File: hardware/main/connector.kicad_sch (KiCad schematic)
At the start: 22 parts, among them J11 TF-01A, J3 Conn_01x04, J4 Conn_01x04, J5 Conn_01x04, J6 Conn_01x04, J7 Conn_01x10, J7b Conn_01x08, J8 Conn_01x06, J9 Conn_01x04

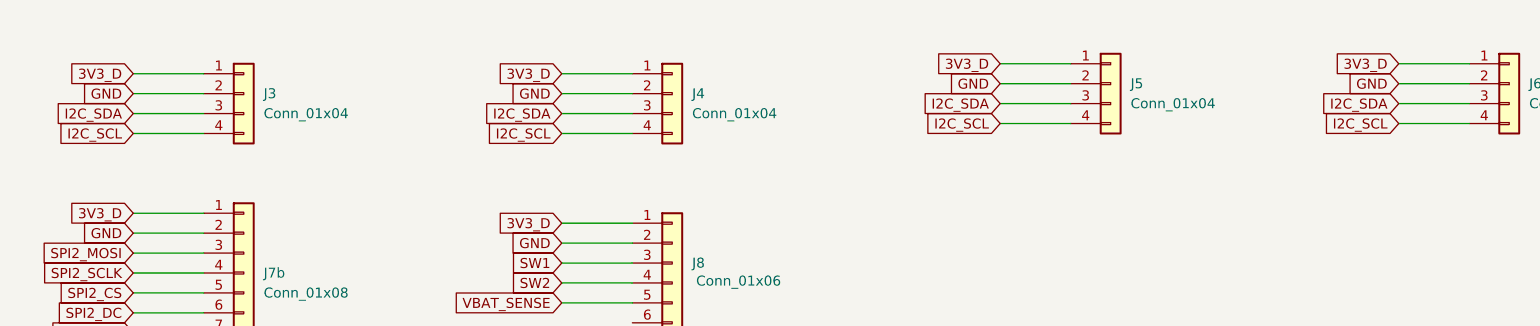
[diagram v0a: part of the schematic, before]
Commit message: hardware+tools: brochage Qwiic J3-J6 applique, outils de verification
- connector.kicad_sch : patch Qwiic reporte dans le projet (pin 1 = GND,
  2 = 3V3_D, 3 = SDA, 4 = SCL). Verifie par netlist sur les 4 connecteurs.
  Solde le point bloquant H2 de l'audit 2026-09-23.
- tools/kicad_netlist.py : reconstruit la netlist depuis les .kicad_sch
  (wires, junctions, global labels, pins transformees). Le script de l'audit
  n'avait pas ete commite et avait ete perdu ; il l'est desormais.
  91,9 % des 430 pins raccordees, 123 nets. Options --ref / --net / --all.
- tools/pdf_text.py : extraction de texte PDF en stdlib seule (ni poppler ni
  pypdf dans le container), avec decodage du kerning TJ — sans quoi les
  datasheets Murata/PUI sortent avec une lettre par mot. Sert la regle
  « datasheet d'abord ».

Co-Authored-By: Claude Opus 5 <noreply@anthropic.com>
Claude-Session: https://claude.ai/code/session_01MMaRLhHbueFYg5T2BWU4YW
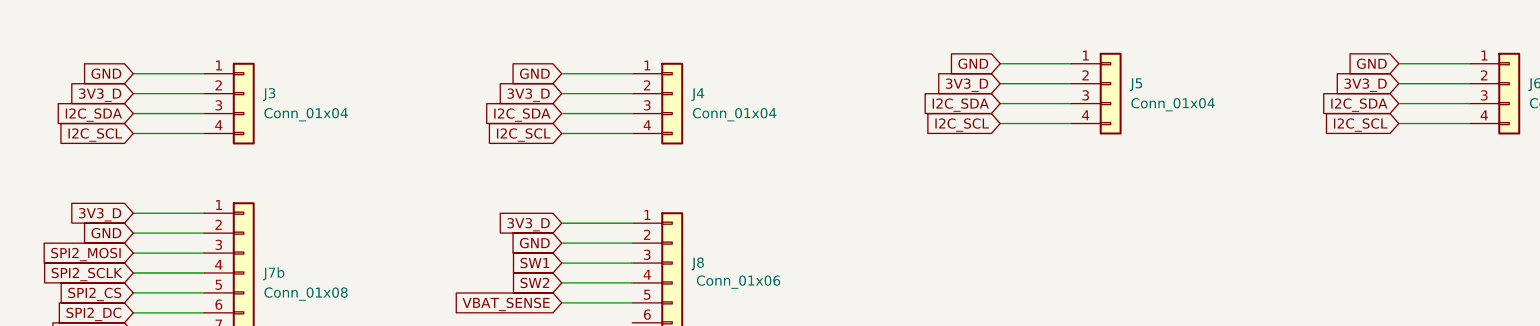
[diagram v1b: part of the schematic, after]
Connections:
- net 3V3_D: now also J3.2 (Pin_2), J4.2 (Pin_2), J5.2 (Pin_2), J6.2 (Pin_2); no longer J3.1 (Pin_1), J4.1 (Pin_1), J5.1 (Pin_1), J6.1 (Pin_1)
- net GND: now also J3.1 (Pin_1), J4.1 (Pin_1), J5.1 (Pin_1), J6.1 (Pin_1); no longer J3.2 (Pin_2), J4.2 (Pin_2), J5.2 (Pin_2), J6.2 (Pin_2)
